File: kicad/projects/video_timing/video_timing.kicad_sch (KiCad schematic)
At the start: 52 parts, among them J1 peripheral_addr_bus_connector, J2 peripheral_aux_connector, J3 peripheral_membank_connector, J4 Conn_01x16_Socket, U1 74HC161, U10 74HC30, U11 74HC30, U12 74HC30, U13 74HC30, U14 74HC30, U15 74HC30, U16 74HC30, U17 74HC30, U18 74HC161, U2 74HC161, U20 74HC11, U21 74HC04, U3 74HC161, U4 74HC161, U5 74HC161, U6 74HC04, U7 74HC04, U8 74HC00, U9 74HC00, X1 CXO_DIP8

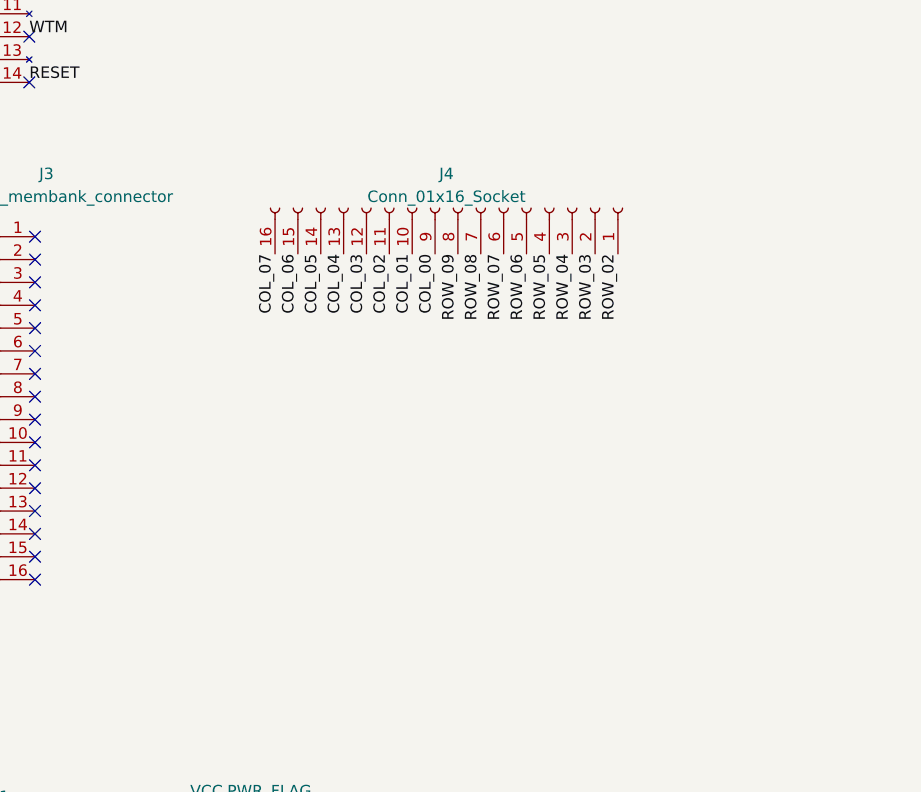
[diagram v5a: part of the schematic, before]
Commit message: Adding video aux and some bits and bieces on video boards.
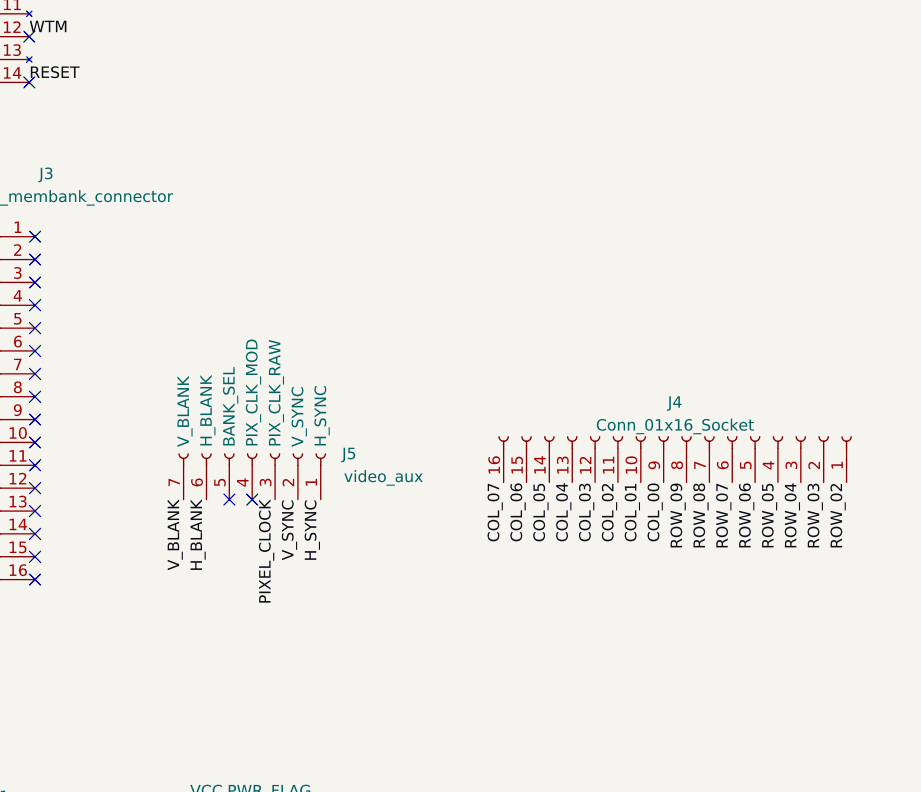
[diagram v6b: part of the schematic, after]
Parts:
- added J5: video_aux, Connector_PinSocket_2.54mm:PinSocket_1x07_P2.54mm_Horizontal, symbol sixteen-bit-computer:video_aux
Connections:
- net H_BLANK: now also J5.6 (H_BLANK)
- net H_SYNC: now also J5.1 (H_SYNC)
- net PIXEL_CLOCK: now also J5.3 (PIX_CLK_RAW)
- net V_BLANK: now also J5.7 (V_BLANK)
- net V_SYNC: now also J5.2 (V_SYNC)
- no-connect marks 67 -> 69
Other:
- moved on the sheet: J4
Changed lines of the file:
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@@
   (paper "C")
   (bus_alias "BANK_BUS" (members "BANK_BUS_00" "BANK_BUS_01" "BANK_BUS_02" "BANK_BUS_03" "BANK_BUS_04" "BANK_BUS_05" "BANK_BUS_06" "BANK_BUS_07" "BANK_BUS_08" "BANK_BUS_09" "BANK_BUS_10" "BANK_BUS_11" "BANK_BUS_12" "BANK_BUS_13" "BANK_BUS_14" "BANK_BUS_15"))
-  (bus_alias "ROW_BUS" (members "ROW_00" "ROW_01" "ROW_02" "ROW_03" "ROW_04" "ROW_05" "ROW_06" "ROW_07" "ROW_08" "ROW_09" "~{ROW_00}" "~{ROW_01}" "~{ROW_02}" "~{ROW_03}" "~{ROW_05}" "~{ROW_08}" "~{ROW_09}" "ROW_05_06_07" "~{ROW_04}"))
-  (bus_alias "ADDR_BUS" (members "ADDR_BUS_00" "ADDR_BUS_01" "ADDR_BUS_02" "ADDR_BUS_03" "ADDR_BUS_04" "ADDR_BUS_05" "ADDR_BUS_06" "ADDR_BUS_07" "ADDR_BUS_08" "ADDR_BUS_09" "ADDR_BUS_10" "ADDR_BUS_11" "ADDR_BUS_12" "ADDR_BUS_13" "ADDR_BUS_14" "ADDR_BUS_15"))
   (bus_alias "COL_BUS" (members "COL_00" "COL_01" "COL_02" "COL_03" "COL_04" "COL_05" "COL_06" "COL_07" "~{COL_00}" "~{COL_01}" "~{COL_02}" "~{COL_03}" "~{COL_04}" "~{COL_05}" "~{COL_06}" "~{COL_07}"))
   (bus_alias "DATA_BUS" (members "DATA_BUS_00" "DATA_BUS_01" "DATA_BUS_02" "DATA_BUS_03" "DATA_BUS_04" "DATA_BUS_05" "DATA_BUS_06" "DATA_BUS_07" "DATA_BUS_08" "DATA_BUS_09" "DATA_BUS_10" "DATA_BUS_11" "DATA_BUS_12" "DATA_BUS_13" "DATA_BUS_14" "DATA_BUS_15"))
+  (bus_alias "ADDR_BUS" (members "ADDR_BUS_00" "ADDR_BUS_01" "ADDR_BUS_02" "ADDR_BUS_03" "ADDR_BUS_04" "ADDR_BUS_05" "ADDR_BUS_06" "ADDR_BUS_07" "ADDR_BUS_08" "ADDR_BUS_09" "ADDR_BUS_10" "ADDR_BUS_11" "ADDR_BUS_12" "ADDR_BUS_13" "ADDR_BUS_14" "ADDR_BUS_15"))
+  (bus_alias "ROW_BUS" (members "ROW_00" "ROW_01" "ROW_02" "ROW_03" "ROW_04" "ROW_05" "ROW_06" "ROW_07" "ROW_08" "ROW_09" "~{ROW_00}" "~{ROW_01}" "~{ROW_02}" "~{ROW_03}" "~{ROW_05}" "~{ROW_08}" "~{ROW_09}" "ROW_05_06_07" "~{ROW_04}"))
   (junction (at 156.845 300.355) (diameter 0) (color 0 0 0 0)
   )
@@
   (no_connect (at 83.185 39.37))
   (no_connect (at 444.5 76.835))
+  (no_connect (at 468.63 103.505))
   (no_connect (at 401.32 109.22))
   (no_connect (at 443.865 57.15))
+  (no_connect (at 466.09 103.505))
   (no_connect (at 401.32 60.96))
   (no_connect (at 401.32 101.6))
@@
     (effects (font (size 1.27 1.27)) (justify right bottom))
   )
-  (label "COL_02" (at 483.87 76.2 270) (fields_autoplaced)
+  (label "COL_02" (at 509.27 101.6 270) (fields_autoplaced)
     (effects (font (size 1.27 1.27)) (justify right bottom))
   )
@@
     (effects (font (size 1.27 1.27)) (justify right bottom))
   )
+  (label "V_SYNC" (at 473.71 103.505 270) (fields_autoplaced)
+    (effects (font (size 1.27 1.27)) (justify right bottom))
+  )
   (label "ROW_08" (at 342.9 140.335 180) (fields_autoplaced)
     (effects (font (size 1.27 1.27)) (justify right bottom))
   )
-  (label "ROW_04" (at 504.19 76.2 270) (fields_autoplaced)
+  (label "ROW_04" (at 529.59 101.6 270) (fields_autoplaced)
     (effects (font (size 1.27 1.27)) (justify right bottom))
   )
@@
     (effects (font (size 1.27 1.27)) (justify left bottom))
   )
+  (label "H_BLANK" (at 463.55 103.505 270) (fields_autoplaced)
+    (effects (font (size 1.27 1.27)) (justify right bottom))
+  )
   (label "~{COL_00}" (at 92.075 137.795 180) (fields_autoplaced)
     (effects (font (size 1.27 1.27)) (justify right bottom))
@@
     (effects (font (size 1.27 1.27)) (justify right bottom))
   )
-  (label "COL_00" (at 488.95 76.2 270) (fields_autoplaced)
+  (label "COL_00" (at 514.35 101.6 270) (fields_autoplaced)
     (effects (font (size 1.27 1.27)) (justify right bottom))
   )
@@
     (effects (font (size 1.27 1.27)) (justify right bottom))
   )
+  (label "V_BLANK" (at 461.01 103.505 270) (fields_autoplaced)
+    (effects (font (size 1.27 1.27)) (justify right bottom))
+  )
   (label "~{ROW_09}" (at 363.22 150.495 0) (fields_autoplaced)
     (effects (font (size 1.27 1.27)) (justify left bottom))
   )
-  (label "COL_05" (at 476.25 76.2 270) (fields_autoplaced)
+  (label "COL_05" (at 501.65 101.6 270) (fields_autoplaced)
     (effects (font (size 1.27 1.27)) (justify right bottom))
   )
@@
     (effects (font (size 1.27 1.27)) (justify right bottom))
   )
-  (label "COL_06" (at 473.71 76.2 270) (fields_autoplaced)
+  (label "COL_06" (at 499.11 101.6 270) (fields_autoplaced)
     (effects (font (size 1.27 1.27)) (justify right bottom))
   )
@@
     (effects (font (size 1.27 1.27)) (justify left bottom))
   )
-  (label "COL_04" (at 478.79 76.2 270) (fields_autoplaced)
+  (label "COL_04" (at 504.19 101.6 270) (fields_autoplaced)
     (effects (font (size 1.27 1.27)) (justify right bottom))
   )
@@
     (effects (font (size 1.27 1.27)) (justify right bottom))
   )
+  (label "PIXEL_CLOCK" (at 471.17 103.505 270) (fields_autoplaced)
+    (effects (font (size 1.27 1.27)) (justify right bottom))
+  )
   (label "~{ROW_INDEX_480}" (at 66.675 229.235 0) (fields_autoplaced)
     (effects (font (size 1.27 1.27)) (justify left bottom))
@@
     (effects (font (size 1.27 1.27)) (justify right bottom))
   )
-  (label "ROW_02" (at 509.27 76.2 270) (fields_autoplaced)
+  (label "ROW_02" (at 534.67 101.6 270) (fields_autoplaced)
     (effects (font (size 1.27 1.27)) (justify right bottom))
   )
@@
     (effects (font (size 1.27 1.27)) (justify left bottom))
   )
-  (label "ROW_09" (at 491.49 76.2 270) (fields_autoplaced)
+  (label "ROW_09" (at 516.89 101.6 270) (fields_autoplaced)
     (effects (font (size 1.27 1.27)) (justify right bottom))
   )
@@
     (effects (font (size 1.27 1.27)) (justify right bottom))
   )
-  (label "COL_07" (at 471.17 76.2 270) (fields_autoplaced)
+  (label "COL_07" (at 496.57 101.6 270) (fields_autoplaced)
     (effects (font (size 1.27 1.27)) (justify right bottom))
   )
@@
     (effects (font (size 1.27 1.27)) (justify right bottom))
   )
-  (label "ROW_07" (at 496.57 76.2 270) (fields_autoplaced)
+  (label "ROW_07" (at 521.97 101.6 270) (fields_autoplaced)
     (effects (font (size 1.27 1.27)) (justify right bottom))
   )
@@
     (effects (font (size 1.27 1.27)) (justify right bottom))
   )
-  (label "ROW_08" (at 494.03 76.2 270) (fields_autoplaced)
+  (label "ROW_08" (at 519.43 101.6 270) (fields_autoplaced)
     (effects (font (size 1.27 1.27)) (justify right bottom))
   )
@@
     (effects (font (size 1.27 1.27)) (justify right bottom))
   )
-  (label "COL_01" (at 486.41 76.2 270) (fields_autoplaced)
+  (label "COL_01" (at 511.81 101.6 270) (fields_autoplaced)
     (effects (font (size 1.27 1.27)) (justify right bottom))
   )
@@
     (effects (font (size 1.27 1.27)) (justify left bottom))
   )
-  (label "ROW_06" (at 499.11 76.2 270) (fields_autoplaced)
+  (label "ROW_06" (at 524.51 101.6 270) (fields_autoplaced)
     (effects (font (size 1.27 1.27)) (justify right bottom))
   )
@@
     (effects (font (size 1.27 1.27)) (justify right bottom))
   )
-  (label "COL_03" (at 481.33 76.2 270) (fields_autoplaced)
+  (label "COL_03" (at 506.73 101.6 270) (fields_autoplaced)
     (effects (font (size 1.27 1.27)) (justify right bottom))
   )
@@
     (effects (font (size 1.27 1.27)) (justify right bottom))
   )
-  (label "ROW_03" (at 506.73 76.2 270) (fields_autoplaced)
+  (label "ROW_03" (at 532.13 101.6 270) (fields_autoplaced)
     (effects (font (size 1.27 1.27)) (justify right bottom))
   )
@@
     (effects (font (size 1.27 1.27)) (justify left bottom))
   )
-  (label "ROW_05" (at 501.65 76.2 270) (fields_autoplaced)
+  (label "ROW_05" (at 527.05 101.6 270) (fields_autoplaced)
     (effects (font (size 1.27 1.27)) (justify right bottom))
   )
@@
     (effects (font (size 1.27 1.27)) (justify left bottom))
   )
+  (label "H_SYNC" (at 476.25 103.505 270) (fields_autoplaced)
+    (effects (font (size 1.27 1.27)) (justify right bottom))
+  )
   (label "GND" (at 54.61 19.05 0) (fields_autoplaced)
     (effects (font (size 1.27 1.27)) (justify left bottom))
@@
     )
   )
+  (symbol (lib_id "sixteen-bit-computer:video_aux") (at 468.63 98.425 270) (mirror x) (unit 1)
+    (in_bom yes) (on_board yes) (dnp no)
+    (property "Reference" "J5" (at 479.425 98.425 90)
+      (effects (font (size 1.27 1.27)))
+    )
+    (property "Value" "video_aux" (at 483.235 100.965 90)
+      (effects (font (size 1.27 1.27)))
+    )
+    (property "Footprint" "Connector_PinSocket_2.54mm:PinSocket_1x07_P2.54mm_Horizontal" (at 468.63 98.425 0)
+      (effects (font (size 1.27 1.27)) hide)
+    )
+    (property "Datasheet" "~" (at 468.63 98.425 0)
+      (effects (font (size 1.27 1.27)) hide)
+    )
+    (pin "1")
+    (pin "2")
+    (pin "3")
+    (pin "4")
+    (pin "5")
+    (pin "6")
+    (pin "7")
+    (instances
+      (project "video_timing"
+        (path "/0c25b387-1696-4e3f-ab8e-df646088b074"
+          (reference "J5") (unit 1)
+        )
+      )
+    )
+  )
   (symbol (lib_id "sixteen-bit-computer:74HC30") (at 277.495 287.655 0) (unit 2)
     (in_bom yes) (on_board yes) (dnp no)
@@
     )
   )
-  (symbol (lib_id "Connector:Conn_01x16_Socket") (at 491.49 71.12 270) (mirror x) (unit 1)
+  (symbol (lib_id "Connector:Conn_01x16_Socket") (at 516.89 96.52 270) (mirror x) (unit 1)
     (in_bom yes) (on_board yes) (dnp no)
-    (property "Reference" "J4" (at 490.22 67.31 90)
+    (property "Reference" "J4" (at 515.62 92.71 90)
       (effects (font (size 1.27 1.27)))
     )
-    (property "Value" "Conn_01x16_Socket" (at 490.22 69.85 90)
+    (property "Value" "Conn_01x16_Socket" (at 515.62 95.25 90)
       (effects (font (size 1.27 1.27)))
     )
-    (property "Footprint" "Connector_PinSocket_2.54mm:PinSocket_1x16_P2.54mm_Horizontal" (at 491.49 71.12 0)
+    (property "Footprint" "Connector_PinSocket_2.54mm:PinSocket_1x16_P2.54mm_Horizontal" (at 516.89 96.52 0)
       (effects (font (size 1.27 1.27)) hide)
     )
-    (property "Datasheet" "~" (at 491.49 71.12 0)
+    (property "Datasheet" "~" (at 516.89 96.52 0)
       (effects (font (size 1.27 1.27)) hide)
     )

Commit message: Start PCB for video timing.
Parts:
- removed C1: C, Capacitor_THT:C_Disc_D5.0mm_W2.5mm_P5.00mm, symbol Device:C
- removed R1: R_US, Resistor_THT:R_Axial_DIN0207_L6.3mm_D2.5mm_P10.16mm_Horizontal, symbol Device:R_US
- added TP2, TP3, TP4, TP5, TP6: TestPoint, Connector_Pin:Pin_D1.0mm_L10.0mm, symbol Connector:TestPoint
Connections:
- net GND: now also U6.1, TP6.1
- net H_BLANK: now also TP2.1
- net H_SYNC: now also TP4.1
- net PIXEL_CLOCK: now also TP3.1; no longer U6.1
- net V_BLANK: now also TP1.1
- net V_SYNC: now also TP5.1
- net ~{PIXEL_CLOCK}: no longer names the net of U6.2
- no-connect marks 69 -> 70
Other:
- moved on the sheet: TP1, U6A
